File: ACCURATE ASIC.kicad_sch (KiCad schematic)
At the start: 65 parts, among them IC1 CERN_aCCURATE2_A_Chip1, IC2 AD817ARZ, IC3 DAC7578SRGE, IC4 AD817ARZ, IC5 AD817ARZ, J14 Conn_01x03, J18 Conn_02x03_Odd_Even, SW1 HARWIN_M50-1900005, SW2 HARWIN_M50-1900005

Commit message: Updated template, readded FPGA prog conn
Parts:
- removed D1 (x3): SMBJ3V3, ICs And Semiconductors SMD:DIOM5436X244N, symbol Diodes:SMBJ3V3
- removed J14: Conn_01x03, Connector_PinHeader_2.54mm:PinHeader_1x03_P2.54mm_Vertical, symbol Connector_Generic:Conn_01x03
- removed SW1: HARWIN_M50-1900005, symbol HARWIN:HARWIN_M50-1900005
- added C11, C59: CC0603_100NF_50V_10%_X7R, Capacitors SMD:CAPC1608X87N, symbol Capacitors SMD:CC0603_100NF_50V_10%_X7R
- added C58: CC0603_10UF_25V_20%_X5R, Capacitors SMD:CAPC1709X100N, symbol Capacitors SMD:CC0603_10UF_25V_20%_X5R
- added IC9: AD817ARZ, ICs And Semiconductors SMD:SOIC127P600X175-8N, symbol Operational Amplifiers:AD817ARZ
- added U1: SHT4x, Sensor_Humidity:Sensirion_DFN-4_1.5x1.5mm_P0.8mm_SHT4x_NoCentralPad, symbol Sensor_Humidity:SHT4x
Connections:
- net CLK is gone; now on net FPGA_CLK: IC1.19
- net +3V3D: now also C11.1, U1.3 (VDD)
- net +5V: now also C58.1, C59.1, IC9.7 (V+)
- net GND: now also C11.2, C58.2, C59.2, IC9.4 (V-), U1.4 (VSS)
- net MCU_SCL: now also U1.2 (SCL)
- net MCU_SDA: now also U1.1 (SDA)
- net OTA_Out: now also IC9.3 (IN+)
- new net OTA_Out_Buf: IC9.2 (IN-), IC9.6 (OUT)
- no-connect marks 20 -> 21
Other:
- note added: "Humidity and Temperature sensor"
- note added: "OTA ADC"
- note removed: "FPGA/External Clock Header"
- moved on the sheet: C1, C10, C2, C22, C23, C24, C25, C3, C4, C5, C6, C67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

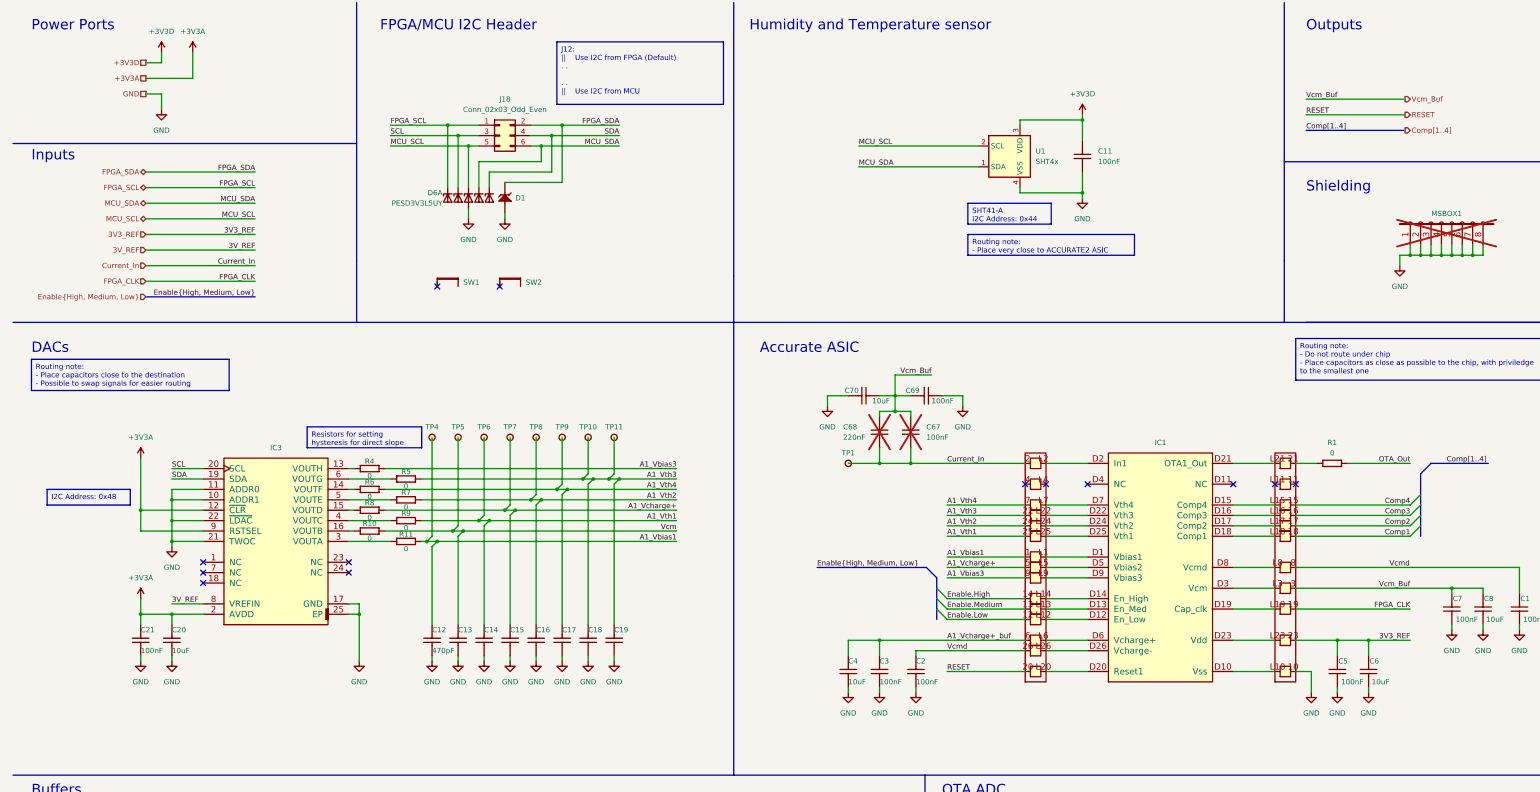
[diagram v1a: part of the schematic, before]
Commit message: Split I2C buses, FPGA2MCU has its own now
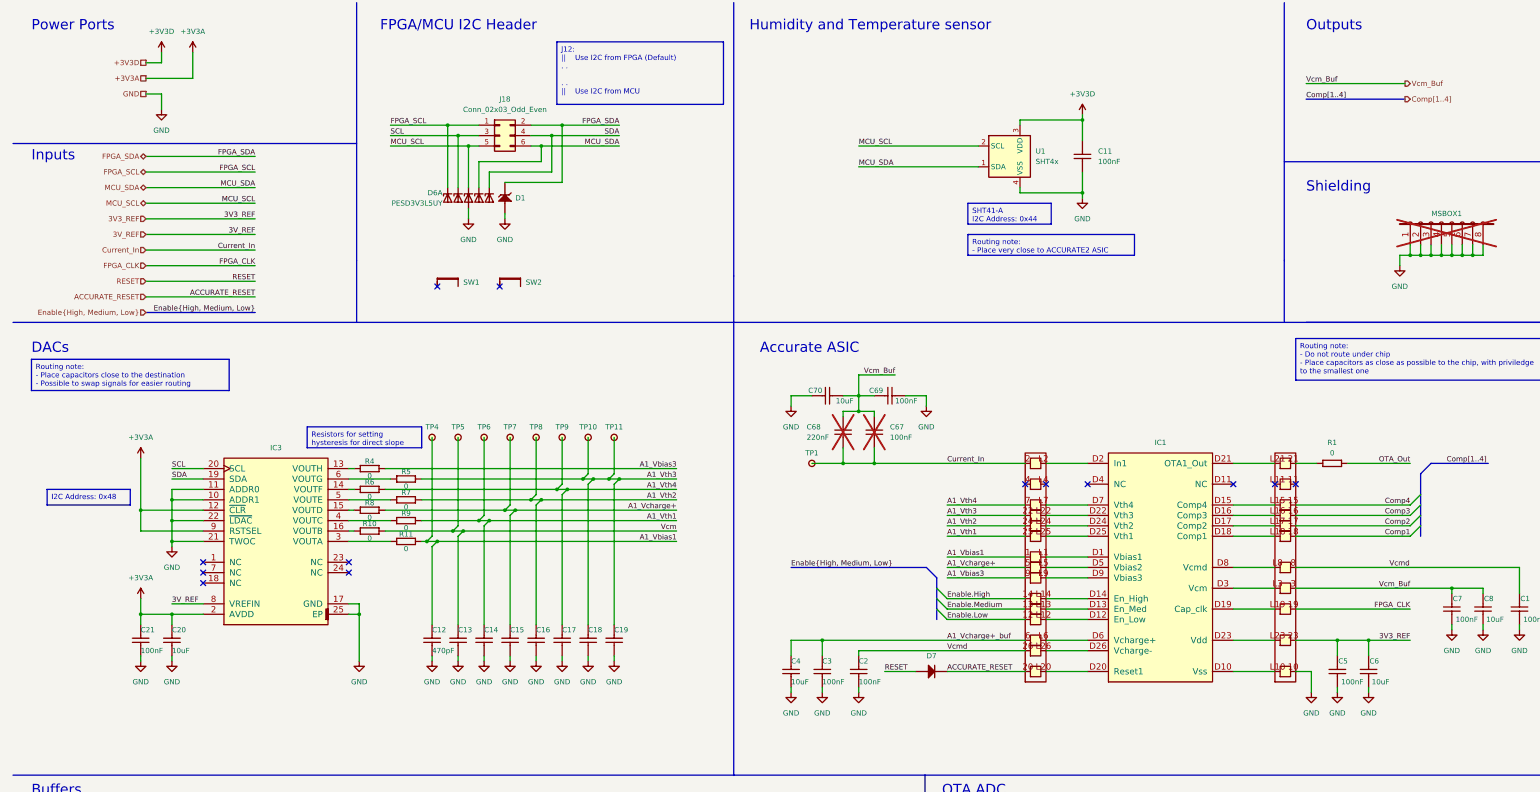
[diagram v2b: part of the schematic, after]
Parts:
- added D7: 1N4148WS, Diode_THT:D_DO-41_SOD81_P7.62mm_Horizontal, symbol Diodes:1N4148WS
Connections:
- net RESET: now also D7.2 (A); no longer IC1.20
- new net ACCURATE_RESET: D7.1 (C), IC1.20
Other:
- moved on the sheet: C2, C3, C4, C67, C68, C69, C70, TP1

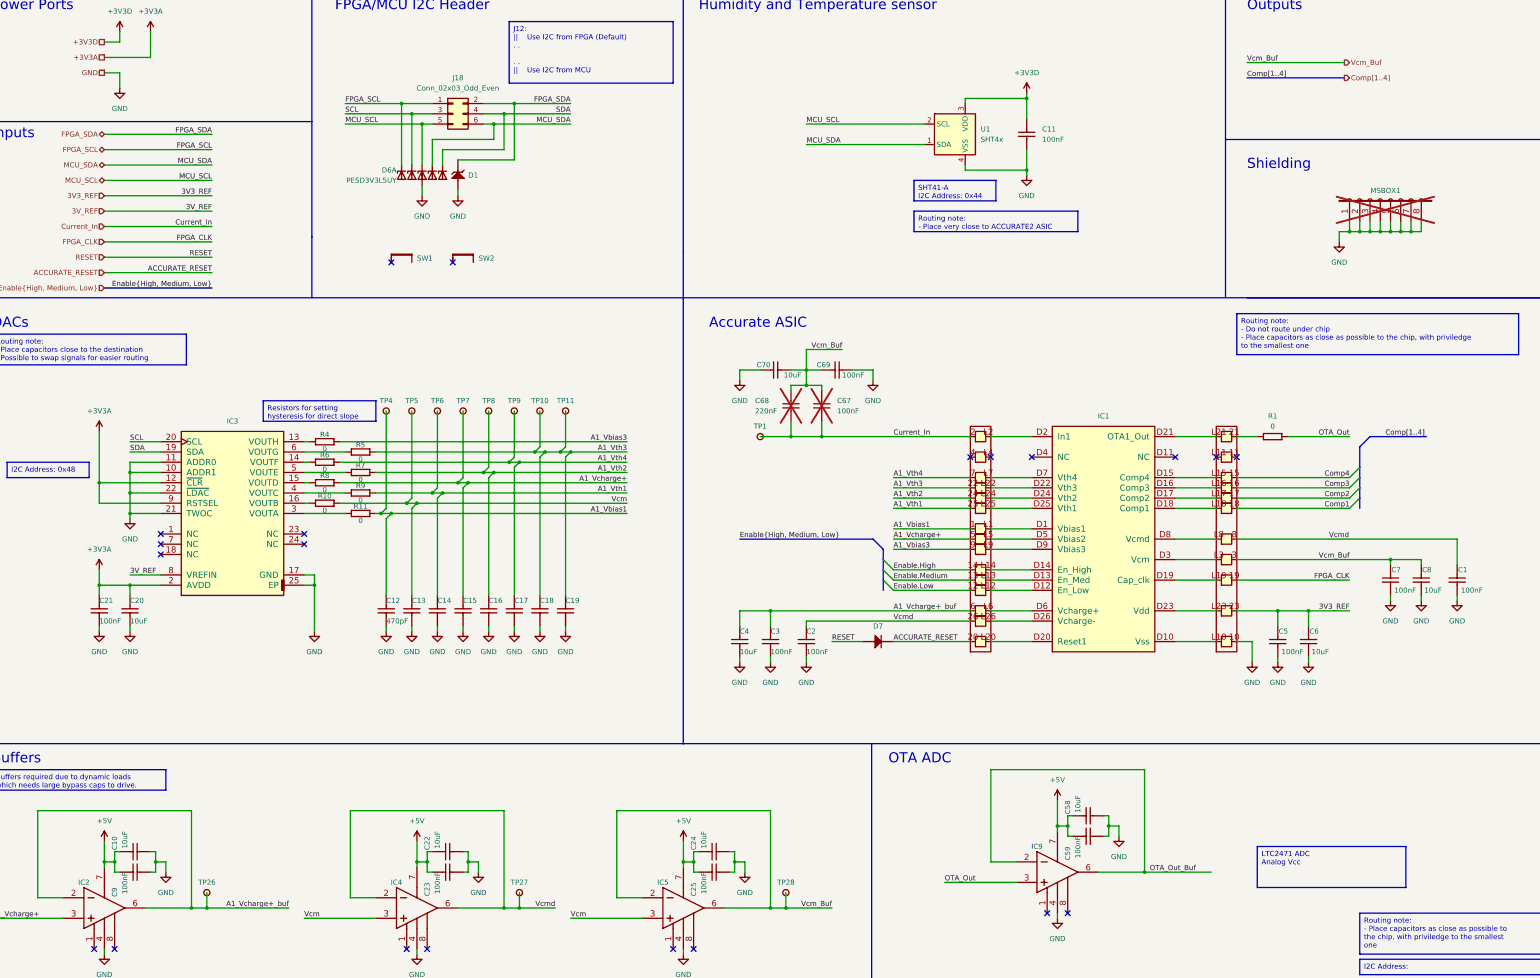
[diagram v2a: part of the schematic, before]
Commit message: Reannotated schematic, added PSU calculation, some polish
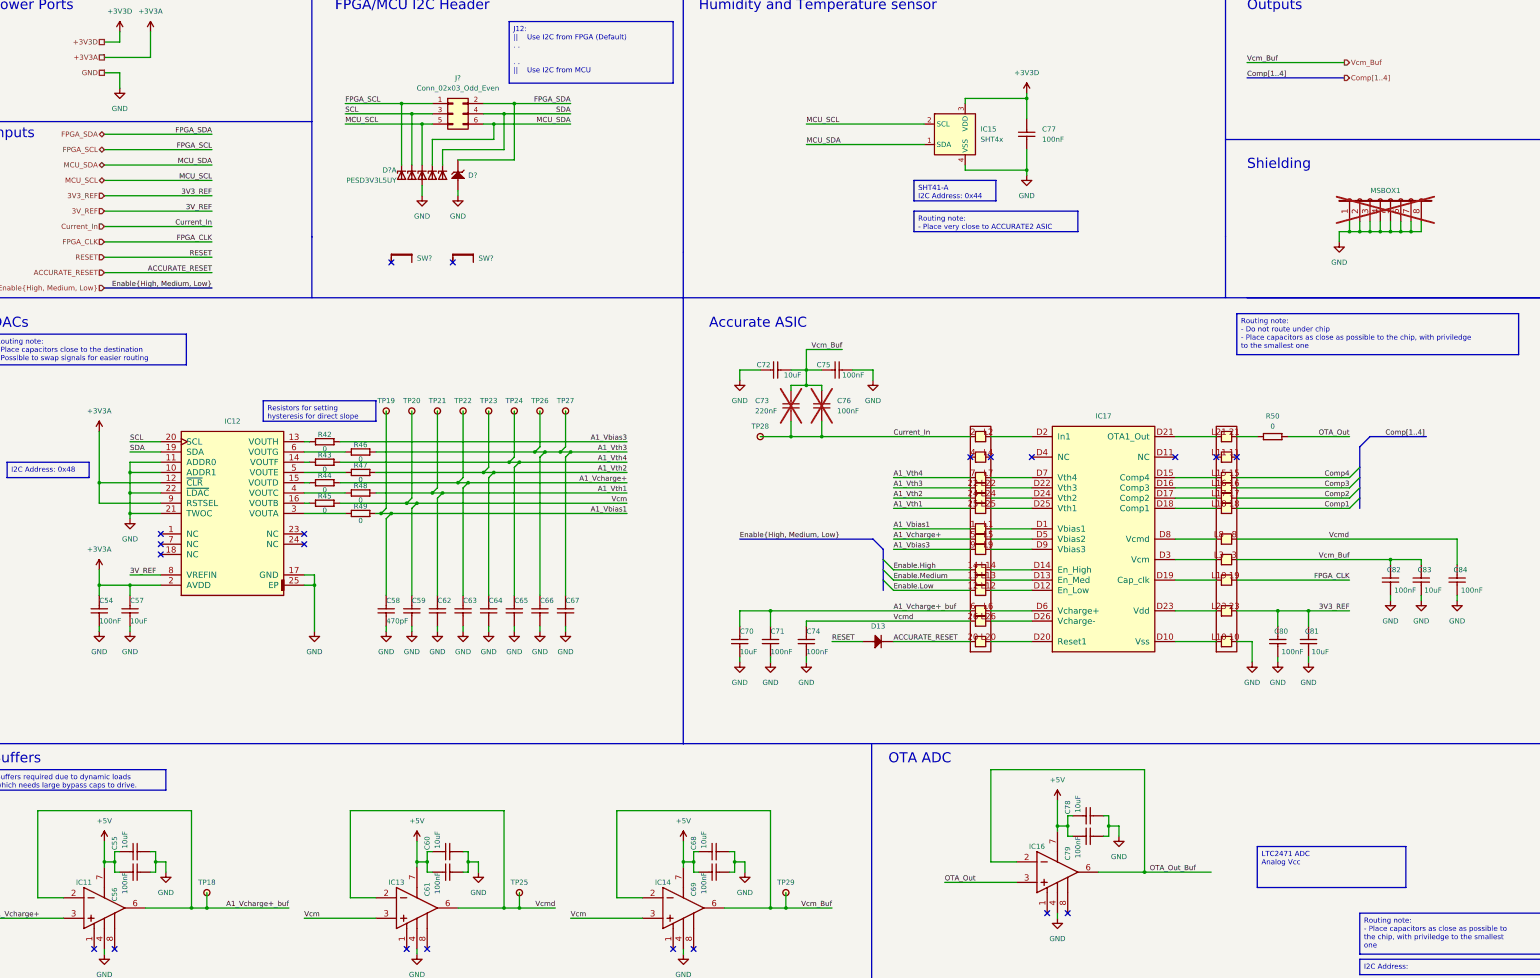
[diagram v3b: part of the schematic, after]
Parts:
- renumbered C21 to C54, C10 to C55, C9 to C56, C20 to C57, C12 to C58, C13 to C59, C22 to C60, C23 to C61, C14 to C62, C15 to C63, C16 to C64, C17 to C65, C18 to C66, C19 to C67, C24 to C68, C25 to C69, C4 to C70, C3 to C71, C70 to C72, C68 to C73, C2 to C74, C69 to C75, C67 to C76, C11 to C77, C58 to C78, C59 to C79, C5 to C80, C6 to C81, C7 to C82, C8 to C83, C1 to C84, D7 to D13, D6 to D?, D1 to D?, IC2 to IC11, IC3 to IC12, IC4 to IC13, IC5 to IC14, U1 to IC15, IC9 to IC16, IC1 to IC17, J18 to J?, R4 to R42, R6 to R43, R8 to R44, R10 to R45, R5 to R46, R7 to R47, R9 to R48, R11 to R49, R1 to R50, SW2 to SW?, SW1 to SW?, TP26 to TP18, TP4 to TP19, TP5 to TP20, TP6 to TP21, TP7 to TP22, TP8 to TP23, TP9 to TP24, TP27 to TP25, TP10 to TP26, TP11 to TP27, TP1 to TP28, TP28 to TP29

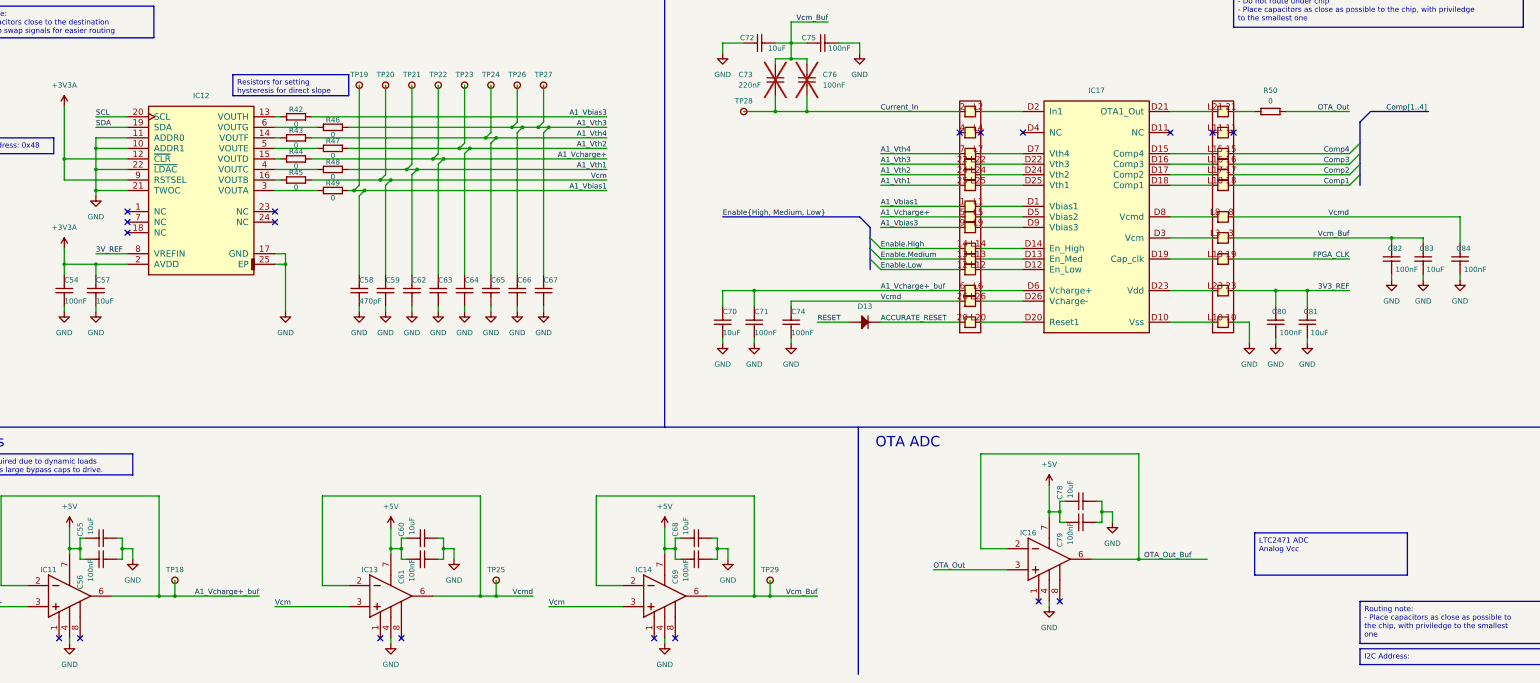
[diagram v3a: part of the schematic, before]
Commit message: Replaced TP1 and FPGA oscillator
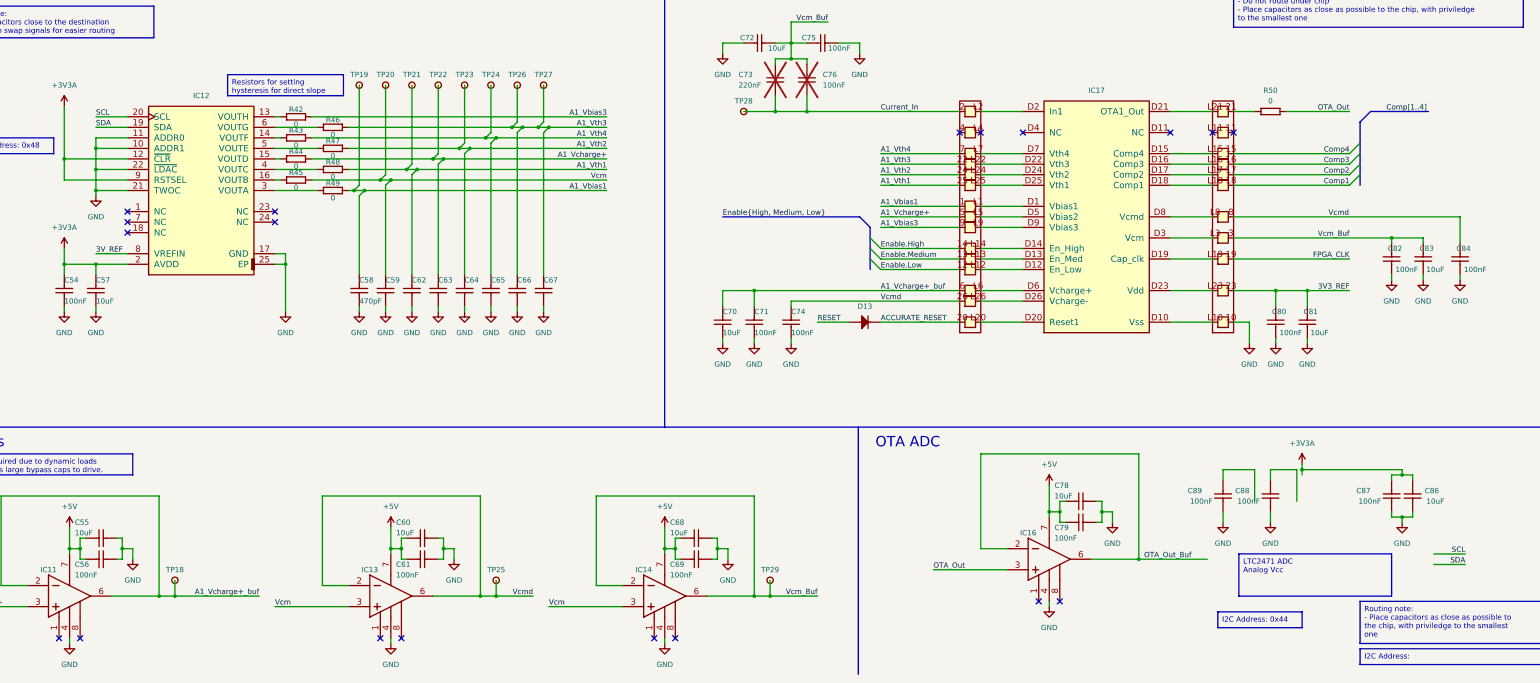
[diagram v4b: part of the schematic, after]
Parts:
- added C86: CC0603_10UF_25V_20%_X5R, Capacitors SMD:CAPC1709X100N, symbol Capacitors SMD:CC0603_10UF_25V_20%_X5R
- added C87, C88, C89: CC0603_100NF_50V_10%_X7R, Capacitors SMD:CAPC1608X87N, symbol Capacitors SMD:CC0603_100NF_50V_10%_X7R
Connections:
- net +3V3A: now also C86.1, C87.1
- net GND: now also C86.2, C87.2, C88.2, C89.2
